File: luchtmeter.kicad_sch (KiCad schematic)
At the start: 70 parts, among them J1 SCHERM, J2 USB-C, J3 I2C, J4 BATTERIJ, Q1 AO3401A, Q2 AO3401A, Q3 AO3400A, Q4 AO3400A, SW1 RESET, SW2 BOOT, SW3 WEKKEN, U1 ESP32-S3-WROOM-1-N16R8, U2 USBLC6-2SC6, U3 XC6220B331MR, U4 LTR-303ALS-01, U5 SCD41-D-R2, U6 SHT45, U7 BQ24075, U8 DW01A

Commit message: Luchtmeter S3 v2: 4.3in Waveshare touchscreen (FFC), all parts on the back, NFC (ST25DV + PCB coil), WROOM-1U, TPS61023 screen boost, case + renders
Co-Authored-By: Claude Opus 5.5 <noreply@anthropic.com>
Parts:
- removed J3: I2C, lucht:JST_SH_SM04B-SRSS-TB_1x04-1MP_P1.00mm_Horizontal, symbol lucht:Conn_01x04_MountingPin
- removed Q1: AO3401A, lucht:SOT-23, symbol lucht:AO3401A
- removed SW3: WEKKEN, lucht:SW_Push_1P1T_NO_CK_KMR2, symbol lucht:SW_Push
- added ANT1: NFC antenne, lucht:NFC_Coil, symbol lucht:L
- added C22: 100n, lucht:C_0603_1608Metric, symbol lucht:C
- added C23: 10p, lucht:C_0603_1608Metric, symbol lucht:C
- added L1: 1uH, lucht:L_Sunlord_MWSA0402S, symbol lucht:L
- added R23, R24: 4k7, lucht:R_0603_1608Metric, symbol lucht:R
- added R25: 100k, lucht:R_0603_1608Metric, symbol lucht:R
- added U10: ST25DV04K, lucht:SOIC-8_3.9x4.9mm_P1.27mm, symbol lucht:ST25DV04K-IER8C3
- added U9: TPS61023, lucht:SOT-563, symbol lucht:TPS61023
- C10: value 1u -> 22u; footprint lucht:C_0603_1608Metric -> lucht:C_0805_2012Metric; MPN 0603 1u X5R ceramic -> 0805 22u X5R ceramic
- C11, C21, C7: value 10u -> 100n; footprint lucht:C_0805_2012Metric -> lucht:C_0603_1608Metric; MPN 0805 10u X5R ceramic -> 0603 100n X7R ceramic
- C12: value 100n -> 47n; MPN 0603 100n X7R ceramic -> 0603 47n X7R ceramic
- C13, C14, C19, C9: value 100n -> 10u; footprint lucht:C_0603_1608Metric -> lucht:C_0805_2012Metric; MPN 0603 100n X7R ceramic -> 0805 10u X5R ceramic
- C15: value 4u7 -> 22u; MPN 0805 4u7 X5R ceramic -> 0805 22u X5R ceramic
- C16: value 10u -> 22u; MPN 0805 10u X5R ceramic -> 0805 22u X5R ceramic
- C17: value 4u7 -> 1u; footprint lucht:C_0805_2012Metric -> lucht:C_0603_1608Metric; MPN 0805 4u7 X5R ceramic -> 0603 1u X5R ceramic
- C20: value 47n -> 100n; MPN 0603 47n X7R ceramic -> 0603 100n X7R ceramic
- C4: value 10u -> 4u7; MPN 0805 10u X5R ceramic -> 0805 4u7 X5R ceramic
- C5: value 22u -> 10u; MPN 0805 22u X5R ceramic -> 0805 10u X5R ceramic
- C6: value 100n -> 4u7; footprint lucht:C_0603_1608Metric -> lucht:C_0805_2012Metric; MPN 0603 100n X7R ceramic -> 0805 4u7 X5R ceramic
- D1: value groen -> rood laden; MPN LED 0603 green (status) -> LED 0603 red (charging)
- D2: value rood laden -> groen USB; MPN LED 0603 red (charging) -> LED 0603 green (USB power)
- H1, H2, H3, H4: value M3 -> M2; footprint lucht:MountingHole_3.2mm_M3 -> lucht:MountingHole_2.2mm_M2
- J1: footprint lucht:PinSocket_1x14_P2.54mm_Vertical -> lucht:Hirose_FH12-40S-0.5SH_1x40-1MP_P0.50mm_Horizontal; symbol lucht:Conn_01x14 -> lucht:Conn_01x40_MountingPin; MPN 1x14 female header 2.54 mm, 8.5 mm high (for the MSP2807 2.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 -> Hirose FH12-40S-0.5SH(55): 40-pin 0.5 mm FFC to the Wavesha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
- J4: MPN solder pads for the 18650 leads (18 AWG) -> solder pads for the LiPo leads
- Q2: MPN AO3401A (load switch display + sensors) -> AO3401A (load switch: sensors + NFC)
- R10: value 100k -> 100; MPN 0603 100k 1% -> 0603 100 1%
- R11: value 3.6k -> 1k; MPN 0603 3.6k 1% (charge current ~250 mA for a 300 mAh LiPo; 1k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 -> 0603 1k 1%
- R12: value 1.1k -> 1M; MPN 0603 1.1k 1% (input limit ~1.4 A) -> 0603 1M 1% (battery voltage / 2)
- R13: value 10k -> 1M; MPN 0603 10k 1% (TS: no NTC, fixed 10k) -> 0603 1M 1%
- R15: value 100k -> 10k; MPN 0603 100k 1% -> 0603 10k 1%
- R16: value 1k -> 732k; MPN 0603 1k 1% -> 0603 732k 1%
- R17: value 100 -> 100k; MPN 0603 100 1% -> 0603 100k 1%
- R18: value 1k -> 100k; MPN 0603 1k 1% -> 0603 100k (screen off at boot / in sleep)
- R19: value 1M -> 10k; MPN 0603 1M 1% (battery voltage) -> 0603 10k (GT911 power-on reset)
- R20: value 1M -> 10k; MPN 0603 1M 1% -> 0603 10k (INT low at reset -> GT911 address 0x5D)
- R21: value 100k -> 4k7; MPN 0603 100k 1% -> 0603 4k7 1%
- R22: value 10k -> 4k7; MPN 0603 10k 1% -> 0603 4k7 1%
- R3: value 1k -> 5k1; MPN 0603 1k 1% -> 0603 5k1 1%
- R5: value 5k1 -> 3.6k; MPN 0603 5k1 1% -> 0603 3.6k 1% (charge ~250 mA; 1k = 0.9 A)
- R6: value 10k -> 1.1k; MPN 0603 10k 1% -> 0603 1.1k 1% (input limit ~1.4 A)
- R7: MPN 0603 10k 1% -> 0603 10k 1% (TS: fixed 10k, no NTC)
- R8, R9: value 4k7 -> 1k; MPN 0603 4k7 1% -> 0603 1k 1%
- SW1: value RESET -> WEKKEN; MPN CK KMR221G (4.2x2.8 tact) -> CK KMR221G: wake from deep sleep (= BOOT when held at reset)
- SW2: value BOOT -> RESET; MPN CK KMR221G (4.2x2.8 tact) -> CK KMR221G
- U1: value ESP32-S3-WROOM-1-N16R8 -> ESP32-S3-WROOM-1U-N16R8; footprint lucht:ESP32-S3-WROOM-1 -> lucht:ESP32-S3-WROOM-1U; MPN ESP32-S3-WROOM-1-N16R8 -> ESP32-S3-WROOM-1U-N16R8 (U.FL; use a 2.4 GHz flex/dipole an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
- U4: MPN LTR-303ALS-01 (ambient light) -> LTR-303ALS-01 (ambient light, front window)
- U5: MPN Sensirion SCD41-D-R2 (photoacoustic CO2 400-5000 ppm + RH/T) -> Sensirion SCD41-D-R2 (CO2 400-5000 ppm + RH/T), behind the 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
- U6: MPN Sensirion SHT45-AD1B-R2 (+-0.1 C, +-1 %RH) -> Sensirion SHT45-AD1B-R2 (+-0.1 C)
- U7: MPN TI BQ24075RGTR (1.5 A Li-ion charger + power path) -> TI BQ24075RGTR (Li-ion charger + power path)
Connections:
- net 3V3: now also C10.1, C11.1, C12.2, R25.2; no longer C20.2, C5.1, C6.1, R10.1, R15.2, R21.2
- net 3V3_SW: now also C18.1, C19.1, C20.1, C22.1, R23.2, R24.2, U10.8 (VCC); no longer C10.1, C11.1, C12.1, C7.1, C8.1, C9.1, J1.1 (Pin_1), R6.2, R7.2, R8.2, R9.2
- net BATN: now also C7.2; no longer C18.2
- net CC1: now also R3.1; no longer R4.1
- net CC2: now also R4.1; no longer R5.1
- net CHG: now also D1.1 (K); no longer D2.1 (K), R14.1, U1.8 (IO15)
- net CH_ILIM: now also R6.1; no longer R12.1
- net CH_ISET: now also R5.1; no longer R11.1
- net CH_TS: now also R7.1; no longer R13.1
- net DW_CS: now also R11.1; no longer R18.1
- net DW_VCC: now also C7.1, R10.2; no longer C18.1, R17.2
- net ESP_EN: now also SW2.1; no longer SW1.1
- net ESP_IO0: now also SW1.1; no longer SW2.1
- net GND: now also C18.2, C20.2, J1.13 (Pin_13), J1.14 (Pin_14), J1.21 (Pin_21), J1.22 (Pin_22), J1.23 (Pin_23), J1.29 (Pin_29), J1.3 (Pin_3), J1.36 (Pin_36), J1.5 (Pin_5), J1.6 (Pin_6), J1.7 (Pin_7), J1.MP (MountPin), R17.2, R3.2, R6.2, R7.2, C22.2, U10.4 (VSS), U9.4 (GND); no longer C12.2, C7.2, D1.1 (K), J1.2 (Pin_2), R12.2
- net LED_CHG_A: now also D1.2 (A), R8.2; no longer D2.2 (A), R16.2
- net PGOOD: now also D2.1 (K); no longer R15.1, U1.9 (IO16)
- net PWR_EN: now also R15.1, U1.8 (IO15); no longer R22.1, U1.11 (IO18)
- net PWR_G: now also C12.1, R14.1, R15.2; no longer C20.1, R21.1, R22.2
- net VBAT: now also C6.1, R10.1, R12.1; no longer C17.1, R17.1, R19.1
- net VBAT_SENSE: now also C8.1, R12.2, R13.1, U1.39 (IO1); no longer C19.1, R19.2, R20.1, U1.12 (IO8)
- net VBUS: now also C4.1, R9.1; no longer C15.1
- net VSYS: now also C14.1, C5.1, C9.1, R8.1, L1.1, U9.3 (VIN); no longer C16.1, C4.1, R16.1
- net DISP_ON: now reaches U1.10 (IO17)
- net DISP_ON: now also R18.1, U9.2 (EN)
- net LCD_G4: now reaches U1.15 (IO3)
- net LCD_G4: now also J1.17 (Pin_17)
- net LCD_G3: now reaches U1.16 (IO46)
- net LCD_G3: now also J1.16 (Pin_16)
- net LCD_G2: now reaches U1.26 (IO45)
- net LCD_G2: now also J1.15 (Pin_15)
- net LCD_G5: now reaches U1.31 (IO38)
- net LCD_G5: now also J1.18 (Pin_18)
- net LCD_G6: now reaches U1.32 (IO39)
- net LCD_G6: now also J1.19 (Pin_19)
- net LCD_G7: now reaches U1.33 (IO40)
- net LCD_G7: now also J1.20 (Pin_20)
- net LCD_R5: now reaches U1.36 (RXD0)
- net LCD_R5: now also J1.10 (Pin_10)
- net LCD_R6: now reaches U1.37 (TXD0)
- net LCD_R6: now also J1.11 (Pin_11)
- removed net ALS_INT: R7.1, U1.34 (IO41), U4.5 (INT)
- net LCD_BL renamed LCD_B5
- net LCD_B5: now also J1.26 (Pin_26); no longer R6.1
- net LCD_CS renamed DE
- net DE: now also J1.34 (Pin_34); no longer J1.3 (Pin_3)
- net LCD_DC renamed PCLK
- net PCLK: now also J1.30 (Pin_30); no longer J1.5 (Pin_5)
- net LCD_LED renamed LCD_R3
- net LCD_R3: now also U1.34 (IO41)
- net LCD_MISO renamed LCD_B3
- net LCD_B3: now also J1.24 (Pin_24); no longer J1.9 (Pin_9)
- net LCD_MOSI renamed HSYNC
- net HSYNC: now also J1.32 (Pin_32); no longer J1.6 (Pin_6)
- net LCD_RST renamed LCD_B4
- net LCD_B4: now also J1.25 (Pin_25); no longer J1.4 (Pin_4)
- net LCD_SCK renamed VSYNC
- net VSYNC: now also J1.33 (Pin_33); no longer J1.7 (Pin_7)
- net LED_ST renamed LCD_R4
- net LCD_R4: now also J1.9 (Pin_9); no longer R3.1
- removed net LED_ST_A: D1.2 (A), R3.2
- net SCL renamed SCL0
- net SCL0: now also U1.5 (IO5), R24.1, U10.6 (SCL); no longer R9.1, U1.38 (IO2)
- net SDA renamed SDA0
- net SDA0: now also U1.4 (IO4), R23.1, U10.5 (SDA); no longer R8.1, U1.39 (IO1)
- net T_CLK renamed SDA1
- net SDA1: now also J1.37 (Pin_37), R21.1; no longer J1.10 (Pin_10)
- net T_CS renamed LCD_B6
- net LCD_B6: now also J1.27 (Pin_27); no longer J1.11 (Pin_11)
- net T_DIN renamed LCD_R7
- net LCD_R7: now also U1.11 (IO18); no longer U1.6 (IO6)
- removed net T_DO: J1.13 (Pin_13), U1.5 (IO5)
- net T_IRQ renamed LCD_B7
- net LCD_B7: now also J1.28 (Pin_28); no longer J1.14 (Pin_14)
- removed net WAKE: C14.1, R10.2, U1.4 (IO4)
- new net BL_PWM: J1.35 (Pin_35), U1.38 (IO2)
- new net BST_FB: R16.2, R17.1, U9.1 (FB)
- new net BST_SW: L1.2, U9.5 (SW)
- new net LED_PG_A: D2.2 (A), R9.2
- new net NFC_AC0: ANT1.1, C23.1, U10.2 (AC0)
- new net NFC_AC1: ANT1.2, C23.2, U10.3 (AC1)
- new net NFC_GPO: R25.1, U1.9 (IO16), U10.7 (GPO)
- new net SCL1: J1.38 (Pin_38), R22.1, U1.12 (IO8)
- new net TP_3V3: J1.4 (Pin_4), R19.1, R21.2, R22.2
- new net TP_INT: J1.40 (Pin_40), R20.1, U1.6 (IO6)
- new net TP_RST: C17.1, J1.39 (Pin_39), R19.2
- new net V5D: C15.1, C16.1, J1.1 (Pin_1), J1.2 (Pin_2), R16.1, U9.6 (VOUT)
- no-connect marks 18 -> 12
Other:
- note added: "3,3 V + SENSORVOEDING"
- note added: "ESP32-S3 (U.FL ANTENNE)"
- note added: "LUCHTMETER S3 v2.0 - ESP32-S3-WROOM-1U (external antenna) behind a Waveshare 4.3in 800x480 IPS capacitive touchscreen (generated from tools/design.py)"
- note added: "Power: USB-C -> BQ24075 (charge 250 mA, power path) -> LiPo on BAT+/BAT- (DW01A) -> XC6220 3.3 V. Screen 5 V from TPS61023 (DISP_ON IO17 high). Sensors + NFC on 3V3_SW (PWR_EN IO15 low = on)."
- note added: "SCHERM 4.3" (FFC)"
- note added: "SCHERM 5 V (TPS61023)"
- note added: "SENSOREN + NFC (I2C0)"
- note added: "Screen FFC J1 (40p 0.5 mm, RGB565): physical pin k = screen pin 41-k. R3-7 IO41 IO42 IO44 IO43 IO18, G2-7 IO45 IO46 IO3 IO38 IO39 IO40, B3-7 IO13 IO14 IO21 IO47 IO48, PCLK IO9 DE IO10 HSYNC IO11 VSYNC IO12, backlight PWM IO2."
- note added: "Touch GT911 on I2C1 (SDA IO7, SCL IO8, INT IO6, address 0x5D). Sensors + NFC on I2C0 (SDA IO4, SCL IO5): SCD41 0x62, SHT45 0x44, LTR-303 0x29, ST25DV 0x53/0x57/0x2D."
- note added: "Wake from deep sleep: WEKKEN button (IO0) or NFC field (ST25DV GPO -> IO16). Battery voltage = ADC(IO1) x 2."
- note removed: "3,3 V + SCHAKELBARE VOEDING"
- note removed: "Deep sleep: set PWR_EN high (rail off), set all display/I2C pins to input, wake on timer or the WEKKEN button (IO4, ext0). Battery: VBAT = ADC(IO8) x 2. CHG IO15, PGOOD IO16 (low = USB)."
- note removed: "Display MSP2807 (ILI9341): SCK IO12, MOSI IO11, MISO IO13, CS IO10, DC IO9, RST IO14, backlight IO21 (active low). Touch XPT2046: CLK IO7, DIN IO6, DO IO5, CS IO47, IRQ IO48."
- note removed: "ESP32-S3"
- note removed: "LUCHTMETER S3 v1.0 - ESP32-S3 air-quality meter with 2.8in touchscreen, battery powered (generated by tools/build_sch.py from tools/design.py)"
- note removed: "Power: USB-C -> BQ24075 (charge ~0.9 A, power path) -> 18650 on BAT+/BAT- (DW01A protection) -> XC6220 3.3 V. 3V3_SW (display + sensors) on when PWR_EN (IO18) is low."
- note removed: "SCHERM 2.8" ILI9341 + TOUCH"
- note removed: "SENSOREN (I2C)"
- note removed: "Sensors on I2C (SDA IO1, SCL IO2): SCD41 CO2 0x62, SHT45 temp/RH 0x44, LTR-303ALS light 0x29 (INT IO41). Qwiic for extra sensors."
- moved on the sheet: C10, C11, C12, C13, C14, C15, C16, C17, C18, C19, C20, C21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

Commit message: Credit varol56 as co-inventor on silkscreen, schematic and firmware
Co-authored-by: varol56 <74546798+varol56@users.noreply.github.com>
Co-Authored-By: Claude Opus 5.5 <noreply@anthropic.com>
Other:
- company: Kobe Van Robaeys - maakleerplek -> Kobe Van Robaeys & varol56 - maakleerplek
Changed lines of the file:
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@@
 		(date "2026-10-18")
 		(rev "1.0")
-		(company "Kobe Van Robaeys - maakleerplek")
+		(company "Kobe Van Robaeys & varol56 - maakleerplek")
 		(comment 1 "ESP32-S3-WROOM-1U + 4.3in touch + SCD41 + SHT45 + LTR-303 + NFC, LiPo")
 	)

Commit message: Name: Kobe Vanrobaeys (README, silkscreen, schematic, firmware, video)
Co-Authored-By: Claude Opus 5.5 <noreply@anthropic.com>
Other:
- company: Kobe Van Robaeys & varol56 - maakleerplek -> Kobe Vanrobaeys & varol56 - maakleerplek
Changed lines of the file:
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@@
 		(date "2026-10-18")
 		(rev "1.0")
-		(company "Kobe Van Robaeys & varol56 - maakleerplek")
+		(company "Kobe Vanrobaeys & varol56 - maakleerplek")
 		(comment 1 "ESP32-S3-WROOM-1U + 4.3in touch + SCD41 + SHT45 + LTR-303 + NFC, LiPo")
 	)

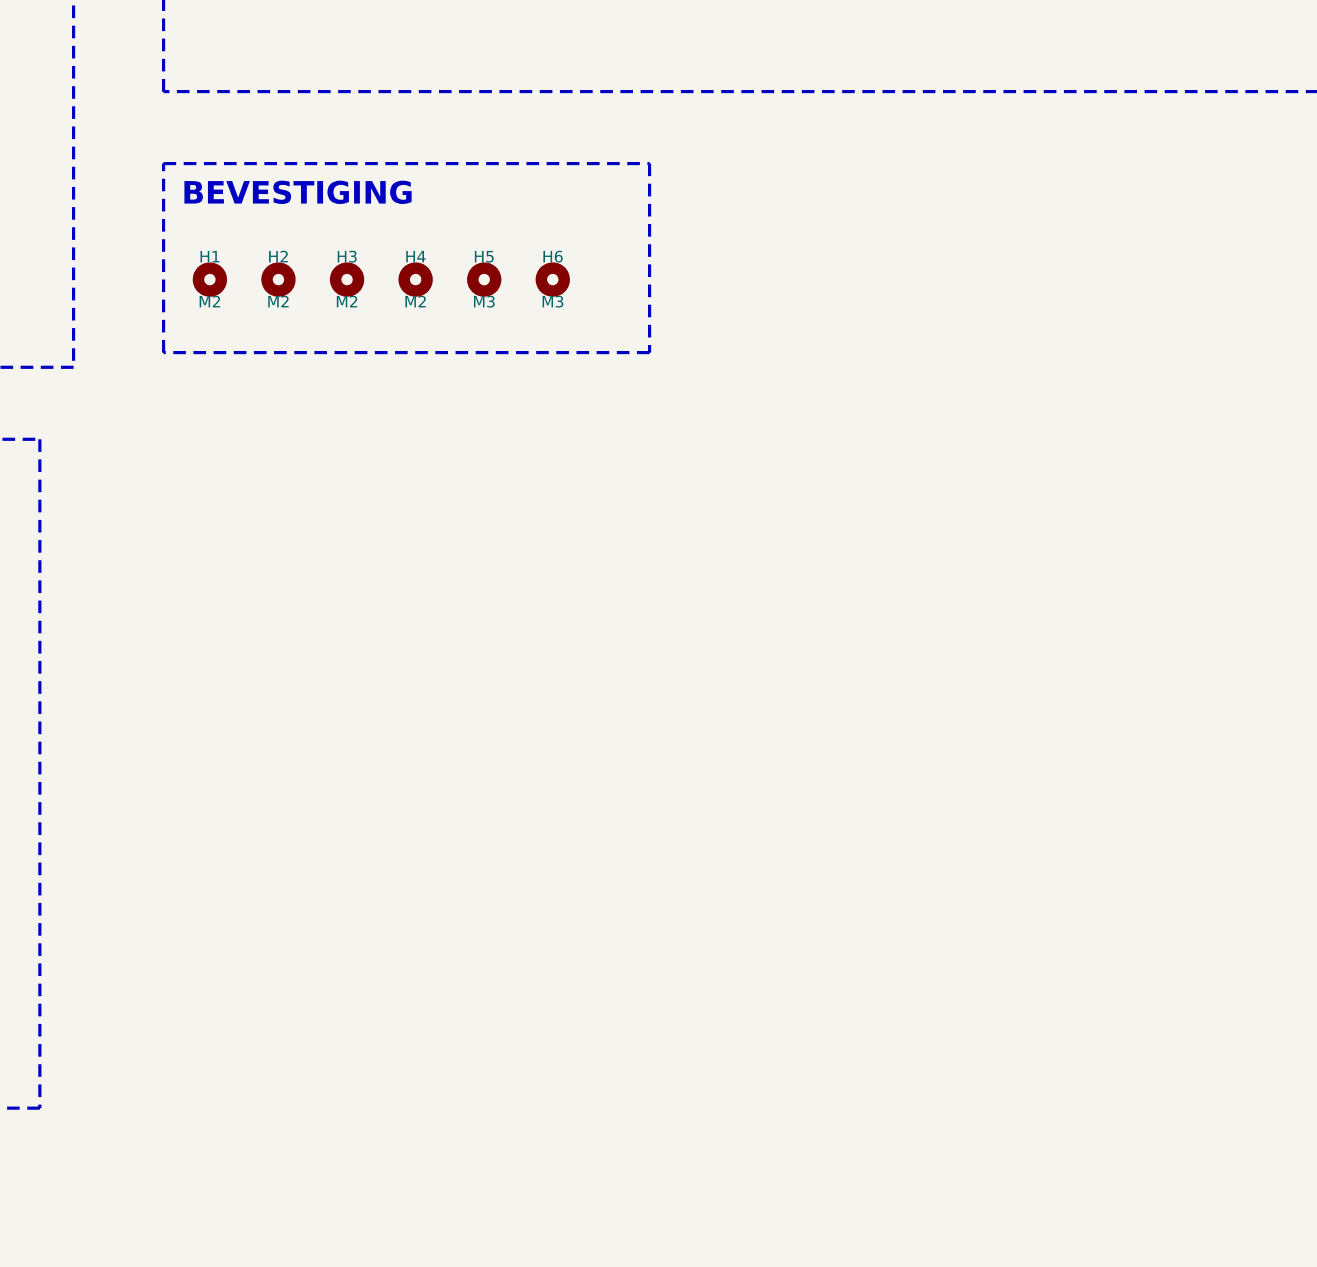
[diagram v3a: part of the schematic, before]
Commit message: Rebuild board, schematic and fab outputs with test points (#1) and J3 (#2)
Regenerated from design.py with KiCad 10.0.7 (flatpak) on Linux:
libs.py, build_sch.py, build_pcb.py, route.sh (Freerouting 2.4.1), finisher,
parity.py fixnc, fab.py.

- TP1-TP13: 1.5 mm test pads in one row on the back, net names in silkscreen
- J3: 1x4 2.54 mm probe connector GND/TP_3V3/SDA1/SCL1 at the left edge next
  to the USB-C (DNP, not in BOM/CPL)

Checks: DRC 0 violations, 0 unconnected, 0 schematic parity issues;
ERC 0 errors 0 warnings; parity.py 314 pads, 0 mismatches. The SHT45 3V3_SW
link is now routed by the tools as well (no manual track).

Co-Authored-By: Claude <noreply@anthropic.com>
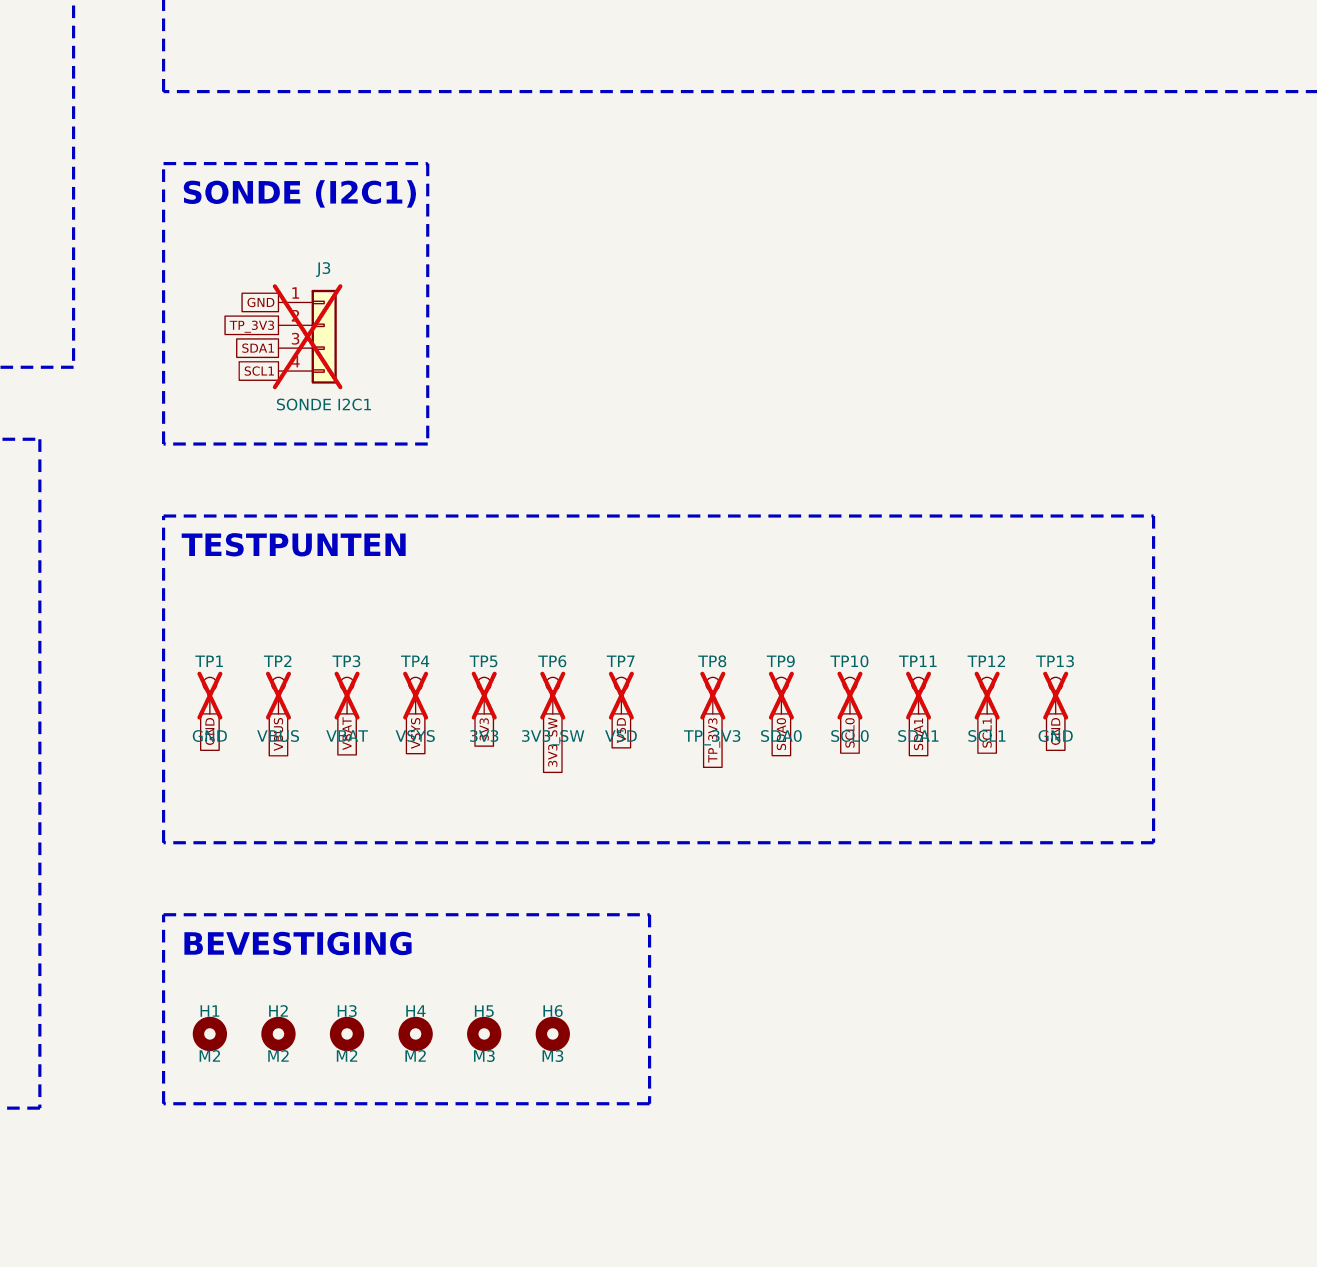
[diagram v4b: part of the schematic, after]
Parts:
- added J3: SONDE I2C1, lucht:PinHeader_1x04_P2.54mm_Vertical, symbol lucht:Conn_01x04
- added TP1, TP13: GND, lucht:TestPoint_Pad_D1.5mm, symbol lucht:TestPoint
- added TP10: SCL0, lucht:TestPoint_Pad_D1.5mm, symbol lucht:TestPoint
- added TP11: SDA1, lucht:TestPoint_Pad_D1.5mm, symbol lucht:TestPoint
- added TP12: SCL1, lucht:TestPoint_Pad_D1.5mm, symbol lucht:TestPoint
- added TP2: VBUS, lucht:TestPoint_Pad_D1.5mm, symbol lucht:TestPoint
- added TP3: VBAT, lucht:TestPoint_Pad_D1.5mm, symbol lucht:TestPoint
- added TP4: VSYS, lucht:TestPoint_Pad_D1.5mm, symbol lucht:TestPoint
- added TP5: 3V3, lucht:TestPoint_Pad_D1.5mm, symbol lucht:TestPoint
- added TP6: 3V3_SW, lucht:TestPoint_Pad_D1.5mm, symbol lucht:TestPoint
- added TP7: V5D, lucht:TestPoint_Pad_D1.5mm, symbol lucht:TestPoint
- added TP8: TP_3V3, lucht:TestPoint_Pad_D1.5mm, symbol lucht:TestPoint
- added TP9: SDA0, lucht:TestPoint_Pad_D1.5mm, symbol lucht:TestPoint
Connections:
- net 3V3: now also TP5.1
- net 3V3_SW: now also TP6.1
- net GND: now also J3.1 (Pin_1), TP1.1, TP13.1
- net SCL0: now also TP10.1
- net SCL1: now also J3.4 (Pin_4), TP12.1
- net SDA0: now also TP9.1
- net SDA1: now also J3.3 (Pin_3), TP11.1
- net TP_3V3: now also J3.2 (Pin_2), TP8.1
- net V5D: now also TP7.1
- net VBAT: now also TP3.1
- net VBUS: now also TP2.1
- net VSYS: now also TP4.1
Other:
- note added: "SONDE (I2C1)"
- note added: "TESTPUNTEN"
- moved on the sheet: H1, H2, H3, H4, H5, H6
